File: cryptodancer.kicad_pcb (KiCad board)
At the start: 2 copper layers, 300 x 137.4 mm, 124 parts, among them SW1 SW_Push, SW10 SW_Push, SW11 SW_Push, SW12 SW_Push, SW13 SW_Push, SW14 SW_Push, SW15 SW_Push, SW16 SW_Push, SW17 SW_Push, SW18 SW_Push, SW19 SW_Push, SW2 SW_Push, SW20 SW_Push, SW21 SW_Push, SW22 SW_Push, SW23 SW_Push, SW24 SW_Push, SW25 SW_Push, SW26 SW_Push, SW27 SW_Push, SW28 SW_Push, SW29 SW_Push, SW3 SW_Push, SW30 SW_Push, SW31 SW_Push, SW32 SW_Push, SW33 SW_Push, SW34 SW_Push, SW35 SW_Push, SW36 SW_Push, SW37 SW_Push, SW38 SW_Push, SW39 SW_Push, SW4 SW_Push, SW40 SW_Push, SW41 SW_Push, SW42 SW_Push, SW43 SW_Push, SW44 SW_Push, SW45 SW_Push, SW46 SW_Push, SW47 SW_Push, SW48 SW_Push, SW49 SW_Push, SW5 SW_Push, SW50 SW_Push, SW51 SW_Push, SW52 SW_Push, SW53 SW_Push, SW54 SW_Push, SW55 SW_Push, SW56 SW_Push, SW57 SW_Push, SW58 SW_Push, SW59 SW_Push, SW6 SW_Push, SW60 SW_Push, SW7 SW_Push, SW8 SW_Push, SW9 SW_Push

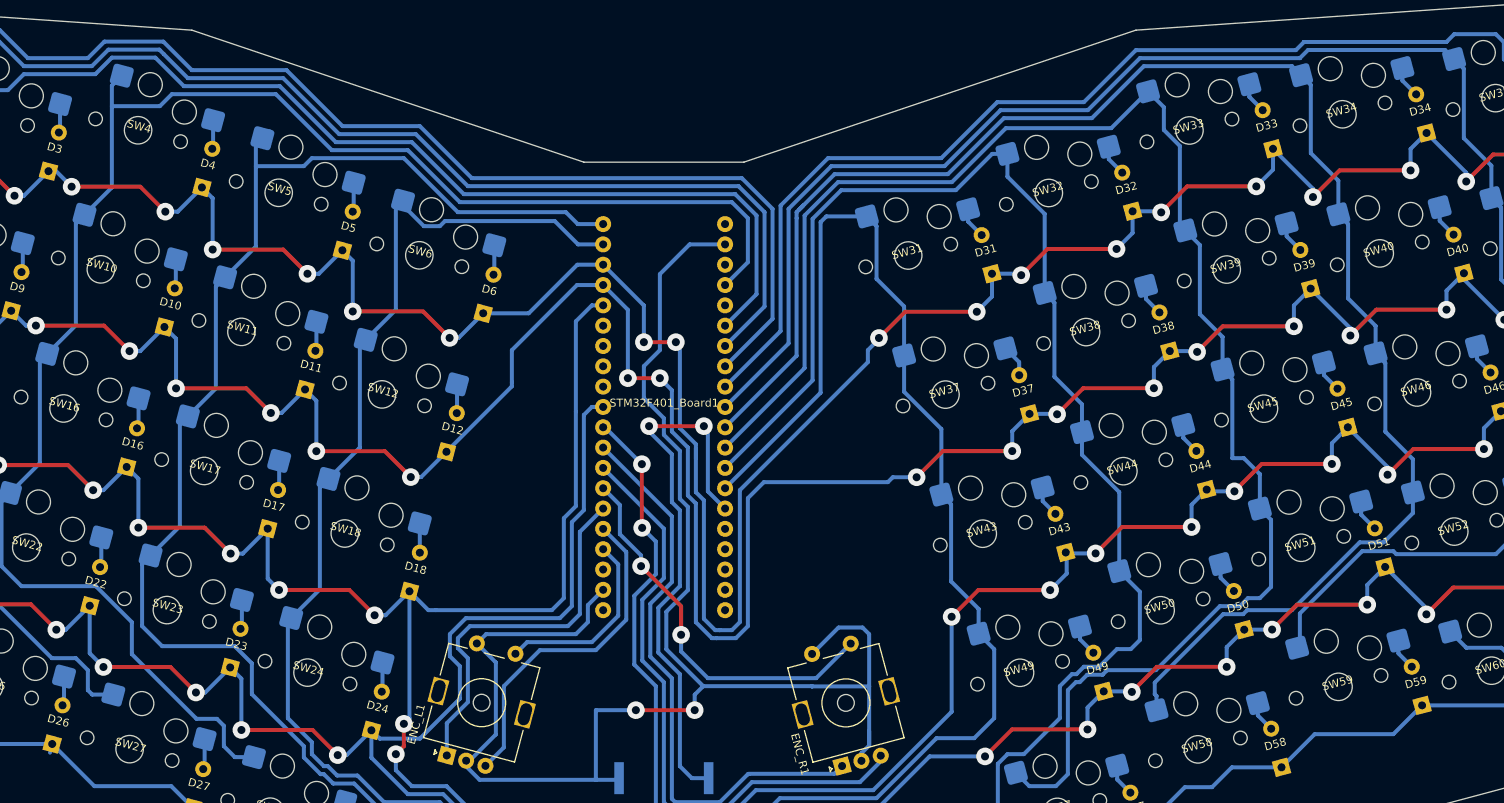
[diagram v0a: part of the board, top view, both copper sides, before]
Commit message: use pin A4 for the buzzer
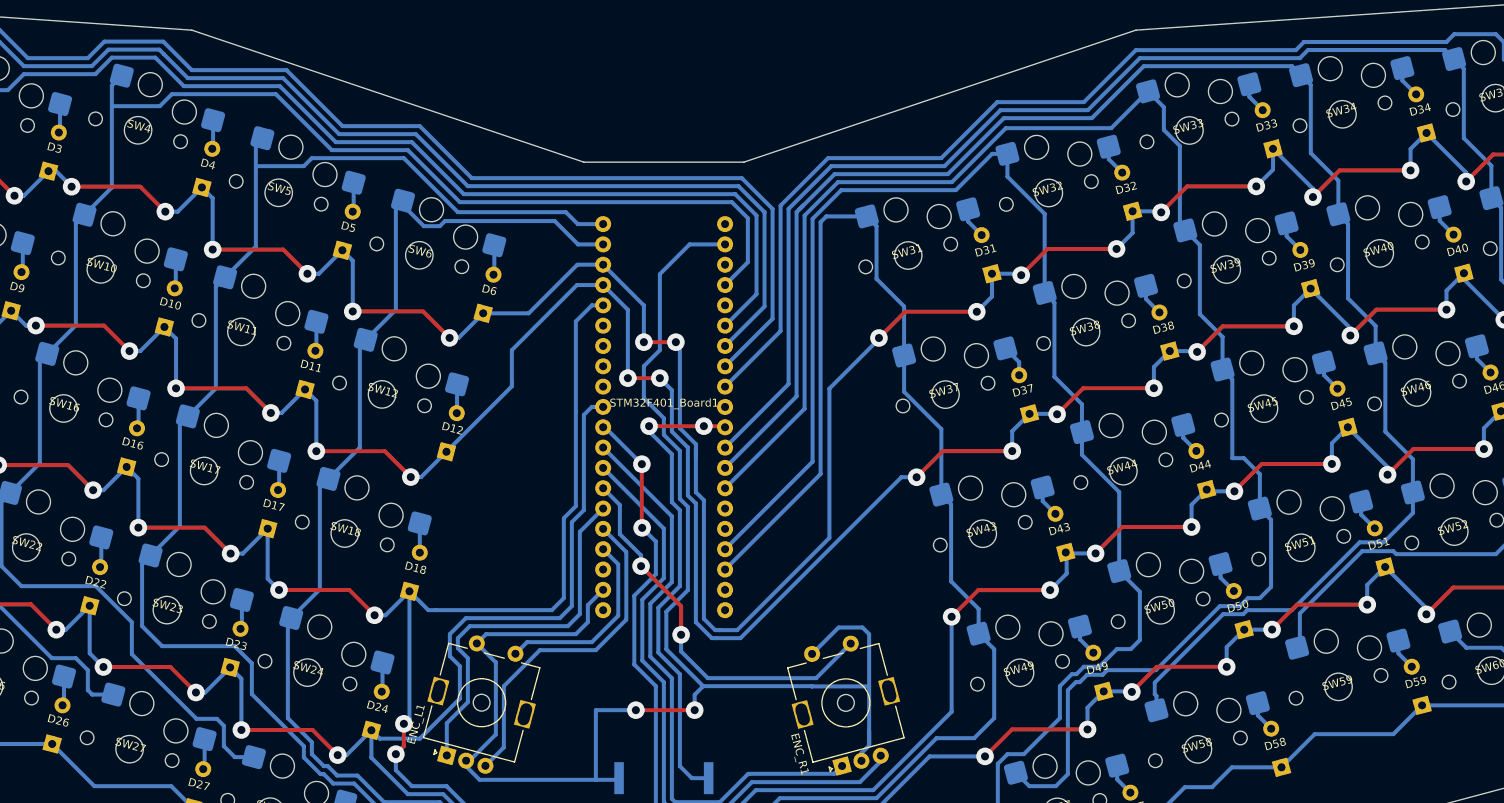
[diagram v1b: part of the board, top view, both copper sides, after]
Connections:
- STM32F401_Board1 pad 30: /col10 -> unconnected-(STM32F401_Board1-A5/SOI8-Pad30)
- STM32F401_Board1 pad 31: /col9 -> /buzz
- STM32F401_Board1 pad 32: /col8 -> /col10
- STM32F401_Board1 pad 33: /col7 -> /col9
- STM32F401_Board1 pad 34: /col6 -> /col8
- STM32F401_Board1 pad 35: /buzz -> unconnected-(STM32F401_Board1-A0/USR-Pad35)
- STM32F401_Board1 pad 37: unconnected-(STM32F401_Board1-C15-Pad37) -> /col7
- STM32F401_Board1 pad 38: unconnected-(STM32F401_Board1-C14-Pad38) -> /col6
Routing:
- net /col7: track 188.3 -> 198.5 mm
- net /col6: track 172.3 -> 182.5 mm
- net /row1: track 414.7 -> 405.3 mm
- net /buzz: track 68.8 -> 60.1 mm
- net /col9: track 207.6 -> 212.7 mm
- net /col10: track 225.2 -> 230.3 mm
- net /col8: track 200.7 -> 205.8 mm
